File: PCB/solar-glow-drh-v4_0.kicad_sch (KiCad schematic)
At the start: 68 parts, among them J1 UPDI hdr, Q2 BSS138LT1G, SW2 LED master, U1 AVR64EA28 (VQFN28), U3 ADXL367, U5 NT3H2211, U6 TPS22919, U7 MB85RC512TY, U8 AEM10300, U9 TPS7A0233PDQNR

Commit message: Q2 + C9 low-profile respins, schematic side -- SOT-523 FET and 1206 C0G
The height ladder above 1.00 (supercaps aside) was C9 1.25 / Q2 1.20 /
U6 1.10. U6 stays (its only flatter variant is a DSBGA, hostile to
rework); these two come down. Both verified against their manufacturers'
own sheets before a field moved, per the U6-pin-map lesson:

Q2: BSS138LT1G (SOT-23, 1.20) -> DMG1012T-7 (SOT523, A1+A2 = 0.90 max,
DS31783 Rev 8-2). Same G/S/D pad order as SOT-23 so the symbol's pin map
carries over -- footprint-only swap for the copper. Electrically a step
up for this job: Vth 0.5-1.0 V (BSS138: 1.5 max) at the 3.3 V gate,
Idss 100 nA max on the drain the harvest budget sees, VGSS +/-6 V
(ESD-protected gate) with margin over the 3.3 V drive. 171k in stock.

C9: QSCT251Q470G1GV001E (0805 High-Q, 1.17 max) -> KGM31BCG2H470GT
(1206 C0G, Kyocera's own table: KGM31 = 3.2x1.6, thickness letter B =
0.94 MAX, and the 47 pF/500 V cell is a B part). Same 47 pF +/-2% -- the
tank tune math in the Description is untouched -- voltage doubles to
500 V, and the raw cap-Q spec drop vs the RF-grade Johanson is
immaterial in-circuit: the tank's loaded Q is coil-dominated. Reuses the
C25-C27 HandSolder land (solarglow:C_1206_3216Metric_HS_LP085), whose
0.95 model covers the 0.94 body -- the package-generic declaration C9's
own part_heights comment already blesses. 1,163 in stock.

The split workflow (fields first, DRH's copper later) now has a home in
the consistency check instead of a red CI: PENDING_FOOTPRINT_SYNC in
check_consistency.py declares the exact (sch_fp, board_fp) pair per ref
with its reason. The declared pair reports as a note; any other mismatch
stays a hard error; and a STALE entry (the board synced, or either side
changed) errors, so the ledger dies in the same commit as the board
round -- the FRONT_SIDE-snapshot shape, again.

Both datasheets fetched to the shelf (Q2 DS31783, C9 C0GNP0-KGM) at
their live prices; availability table regenerated, 29/29 lines OK;
PCB/README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
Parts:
- C9: footprint Capacitor_SMD:C_0805_2012Metric -> solarglow:C_1206_3216Metric_HS_LP085; MPN QSCT251Q470G1GV001E -> KGM31BCG2H470GT; Manufacturer Johanson Technology -> KYOCERA AVX; Supplier P/N 712-QSCT251Q470G1GV001ETR-ND -> 478-KGM31BCG2H470GTCT-ND
- Q2: value BSS138LT1G -> DMG1012T; footprint Package_TO_SOT_SMD:SOT-23 -> Package_TO_SOT_SMD:SOT-523; MPN BSS138LT1G -> DMG1012T-7; Manufacturer onsemi -> Diodes Incorporated; Supplier P/N BSS138LT1GOSCT-ND -> DMG1012T-7DICT-ND
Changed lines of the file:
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@@
 			)
 		)
-		(property "Value" "BSS138LT1G"
+		(property "Value" "DMG1012T"
 			(at 945.94 382.27 0)
 			(show_name no)
@@
 			)
 		)
-		(property "Footprint" "Package_TO_SOT_SMD:SOT-23"
+		(property "Footprint" "Package_TO_SOT_SMD:SOT-523"
 			(at 945.94 387.35 0)
 			(show_name no)
@@
 			)
 		)
-		(property "Description" "N-ch MOSFET SOT-23 -- EN_STO_CH low-side charge-disable buffer: gate<-PA4 (CHG_DIS_G), drain->EN_STO_CH, source->GND (cold-start-deadlock fix)"
+		(property "Description" "N-ch MOSFET SOT-523 (DMG1012T, 0.90 max -- low-profile respin 2026-08-06; was BSS138 SOT-23, 1.20) -- EN_STO_CH low-side charge-disable buffer: gate<-PA4 (CHG_DIS_G), drain->EN_STO_CH, source->GND (cold-start-deadlock fix). Same G/S/D pad order as SOT-23; Vth 1.0 max, Idss 100 nA max, VGSS +/-6 (ESD-protected gate)"
 			(at 934.72 372.11 0)
 			(show_name no)
@@
 			)
 		)
-		(property "MPN" "BSS138LT1G"
+		(property "MPN" "DMG1012T-7"
 			(at 934.72 372.11 0)
 			(show_name no)
@@
 			)
 		)
-		(property "Manufacturer" "onsemi"
+		(property "Manufacturer" "Diodes Incorporated"
 			(at 934.72 372.11 0)
 			(hide yes)
@@
 			)
 		)
-		(property "Supplier P/N" "BSS138LT1GOSCT-ND"
+		(property "Supplier P/N" "DMG1012T-7DICT-ND"
 			(at 934.72 372.11 0)
 			(hide yes)
@@
 			)
 		)
-		(property "Footprint" "Capacitor_SMD:C_0805_2012Metric"
+		(property "Footprint" "solarglow:C_1206_3216Metric_HS_LP085"
 			(at 571.5 129.54 0)
 			(hide yes)
@@
 			)
 		)
-		(property "Description" "NFC tank trim, 0805 high-Q C0G +/-2% (Johanson S-series, ultra-low ESR). PLACED at assembly as of 2026-07-30 - value derived, not trimmed: coil L = 0.958 uH by Greenhouse on the board's 7 rails, ferrite-loaded 1.05-1.30 uH, tag Ci = 50 pF (NT3H2211 Table 42), antenna Cc = 6 pF (AN11276 Table 2). 47 pF lands the enclosed resonance at 14.45 MHz against AN11276 4.2.1's 14.5 MHz single-tag target and stays above the 13.56 carrier across the whole ferrite range. Was 82 pF + DNP, which sat at 12.5 MHz enclosed - under the carrier, the wrong side to miss on."
+		(property "Description" "NFC tank trim, 1206 C0G 500 V +/-2% (Kyocera KGM31B, 0.94 max -- low-profile respin 2026-08-06; was Johanson 0805 High-Q QSCT, 1.17 max: raw cap-Q spec is lower than the RF-grade part but the tank's loaded Q is coil-dominated, and V doubles). PLACED at assembly as of 2026-07-30 - value derived, not trimmed: coil L = 0.958 uH by Greenhouse on the board's 7 rails, ferrite-loaded 1.05-1.30 uH, tag Ci = 50 pF (NT3H2211 Table 42), antenna Cc = 6 pF (AN11276 Table 2). 47 pF lands the enclosed resonance at 14.45 MHz against AN11276 4.2.1's 14.5 MHz single-tag target and stays above the 13.56 carrier across the whole ferrite range. Was 82 pF + DNP, which sat at 12.5 MHz enclosed - under the carrier, the wrong side to miss on."
 			(at 560.07 119.38 0)
 			(hide yes)
@@
 			)
 		)
-		(property "MPN" "QSCT251Q470G1GV001E"
+		(property "MPN" "KGM31BCG2H470GT"
 			(at 560.07 119.38 0)
 			(hide yes)
@@
 			)
 		)
-		(property "Manufacturer" "Johanson Technology"
+		(property "Manufacturer" "KYOCERA AVX"
 			(at 560.07 119.38 0)
 			(hide yes)
@@
 			)
 		)
-		(property "Supplier P/N" "712-QSCT251Q470G1GV001ETR-ND"
+		(property "Supplier P/N" "478-KGM31BCG2H470GTCT-ND"
 			(at 560.07 119.38 0)
 			(hide yes)

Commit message: C9: the Kyocera 1206 falls to the purpose-built answer -- Johanson QSCP 0603
DRH asked for an RF-grade part and widened the search to any case size.
The full-field sweep settled it: Johanson's High-Q family has NO 1206
(the case ladder runs 0201 -> 0603 -> 0805 -> 1111, and the 1111 is a
2.59 mm brick), no maker stocks a purpose-built RF 1206 under 1 mm, and
the uncommon cases (0505, 1111) all start at 1.27 thick. The flat,
+/-2%, >=250 V RF world lives entirely at 0603: Johanson QSCP (0.89),
Murata GQM18 (0.80), Kyocera/ATC 600S (0.89, $2.08).

Picked QSCP251Q470G1GV001T -- the SAME S-series as the QSCT fitted
today (Johanson's own sheet: legacy 251R14S470GV4T, 0603, 250 V,
47 pF +/-2%, thickness max 0.035 in = 0.89 mm), so the tank keeps its
exact pedigree, one case down instead of up. 43,680 in stock, $0.37.
The Kyocera KGM pick from the previous commit is superseded before any
copper moved: sch fields, PENDING_FOOTPRINT_SYNC pair (now 0805 ->
C_0603_1608Metric -- the rework SHRINKS the land, and the board already
hand-works 0603 at C22/C23/FB1/R15/R16), PCB/README row, and the shelf
(KGM sheet culled same-day, git history; JTI part sheet in at the live
price). Value stays 47 pF -- the tune math is untouched.

Availability table regenerated (29/29, C9 verified live); ERC at the
3-hit baseline; consistency 0/0 with the C9 transient re-declared.

Co-Authored-By: Claude Fable 5 <noreply@anthropic.com>
Claude-Session: https://claude.ai/code/session_015D4iTho3BuNxSQyJmyaxvg
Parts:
- C9: footprint solarglow:C_1206_3216Metric_HS_LP085 -> Capacitor_SMD:C_0603_1608Metric; MPN KGM31BCG2H470GT -> QSCP251Q470G1GV001T; Manufacturer KYOCERA AVX -> Johanson Technology; Supplier P/N 478-KGM31BCG2H470GTCT-ND -> 712-QSCP251Q470G1GV001TCT-ND
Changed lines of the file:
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@@
 			)
 		)
-		(property "Footprint" "solarglow:C_1206_3216Metric_HS_LP085"
+		(property "Footprint" "Capacitor_SMD:C_0603_1608Metric"
 			(at 571.5 129.54 0)
 			(hide yes)
@@
 			)
 		)
-		(property "Description" "NFC tank trim, 1206 C0G 500 V +/-2% (Kyocera KGM31B, 0.94 max -- low-profile respin 2026-08-06; was Johanson 0805 High-Q QSCT, 1.17 max: raw cap-Q spec is lower than the RF-grade part but the tank's loaded Q is coil-dominated, and V doubles). PLACED at assembly as of 2026-07-30 - value derived, not trimmed: coil L = 0.958 uH by Greenhouse on the board's 7 rails, ferrite-loaded 1.05-1.30 uH, tag Ci = 50 pF (NT3H2211 Table 42), antenna Cc = 6 pF (AN11276 Table 2). 47 pF lands the enclosed resonance at 14.45 MHz against AN11276 4.2.1's 14.5 MHz single-tag target and stays above the 13.56 carrier across the whole ferrite range. Was 82 pF + DNP, which sat at 12.5 MHz enclosed - under the carrier, the wrong side to miss on."
+		(property "Description" "NFC tank trim, 0603 High-Q C0G 250 V +/-2% (Johanson S-series QSCP, 0.89 max, legacy 251R14S470GV4T -- low-profile respin 2026-08-06, purpose-built RF part kept per DRH: the S-series has NO 1206 case and no maker stocks a flat RF 1206, so the same family one case DOWN. Was the 0805 QSCT, 1.17 max; the 2026-07-30 0402->0805 upsize fled 0402 rework, and 0603 is the board's workhorse hand case). PLACED at assembly as of 2026-07-30 - value derived, not trimmed: coil L = 0.958 uH by Greenhouse on the board's 7 rails, ferrite-loaded 1.05-1.30 uH, tag Ci = 50 pF (NT3H2211 Table 42), antenna Cc = 6 pF (AN11276 Table 2). 47 pF lands the enclosed resonance at 14.45 MHz against AN11276 4.2.1's 14.5 MHz single-tag target and stays above the 13.56 carrier across the whole ferrite range. Was 82 pF + DNP, which sat at 12.5 MHz enclosed - under the carrier, the wrong side to miss on."
 			(at 560.07 119.38 0)
 			(hide yes)
@@
 			)
 		)
-		(property "MPN" "KGM31BCG2H470GT"
+		(property "MPN" "QSCP251Q470G1GV001T"
 			(at 560.07 119.38 0)
 			(hide yes)
@@
 			)
 		)
-		(property "Manufacturer" "KYOCERA AVX"
+		(property "Manufacturer" "Johanson Technology"
 			(at 560.07 119.38 0)
 			(hide yes)
@@
 			)
 		)
-		(property "Supplier P/N" "478-KGM31BCG2H470GTCT-ND"
+		(property "Supplier P/N" "712-QSCP251Q470G1GV001TCT-ND"
 			(at 560.07 119.38 0)
 			(hide yes)

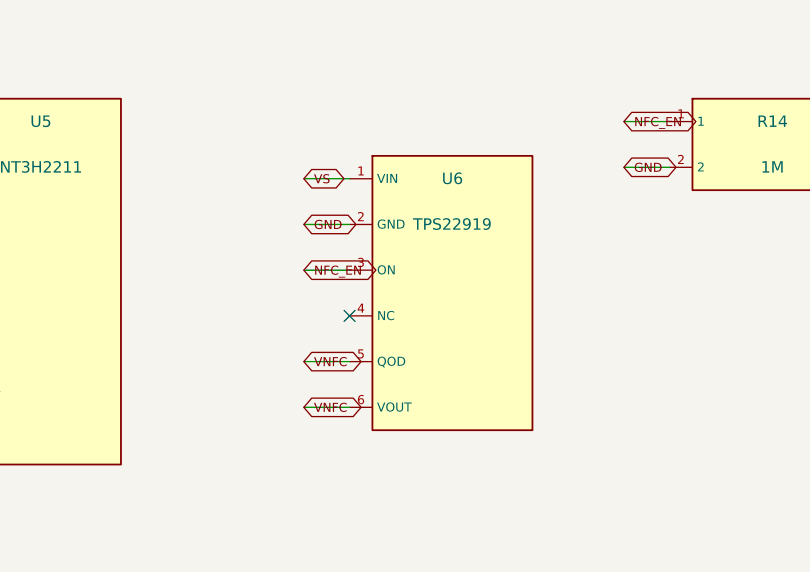
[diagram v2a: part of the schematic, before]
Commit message: U6 goes DSBGA: TPS22916C, 0.5 mm -- every component now clears 1.1 for the ultrathin card
DRH called the swap: with C25-C27 at 0.95, Q2 at 0.90 and C9 at 0.89
pending, U6's SC-70 (1.10) was the last non-supercap part at the 1.1
line, and the ultrathin-card option wants everything UNDER it. The
TPS22919 has no BGA variant (SLVSEN5B lists DCK only); the sibling
that exists for exactly this is the TPS22916 -- TI's ultra-low-leakage
WCSP load switch. C version chosen deliberately: active-high ON, 150R
QOD (the 22919 has QOD; CN/CNL delete it), slow inrush-limited ramp
(the 22919's controlled rise, same idea), plus reverse-current
blocking the 22919 never had.

The honest trade, both sheets side by side: ISD 10 nA typ / 100 nA max
(-40..85) vs the 22919's 2 nA typ -- +8 nA typical on the OFF state the
switch lives in, ~26 nW at 3.3 V -- bought back 16x in ON-state IQ
(0.5 uA vs 8 uA) and 0.6 mm of height. VIN 1-5.5 V, RON 70 mOhm at
3.6 V, ON-pin leakage 10 nA max driven high; R14's 1 M pulldown keeps
the hard-off default either way.

Schematic surgery (the 6-pin symbol dies, a 4-ball one replaces it):
new solarglow:U6_TPS22916 lib def with balls A2/B1/B2/A1 positioned on
the OLD pins 1/2/3/6 canvas points, so the VS/GND/NFC_EN/VNFC wires
never move; the QOD stub wire + its VNFC label deleted (QOD is
internal now) and pin 4's no_connect marker with it -- ERC stays at
the 3-hit baseline, no dangles. The old solarglow:U6 lib def is gone
outright: an unused lib def with part-number defaults is exactly the
bait that sold C1 as an LDO this morning.

Footprint minted from TI's own drawing (solarglow:TPS22916_YFP0004,
4223507/A + SLVSDO5F example layout): 4x diam 0.23 NSMD circles on
0.4 mm pitch, mask +0.05/side, pad-to-pad air 0.17 >= the 0.152 floor,
A1 corner marked on F.Fab. Model chain complete in the same commit:
TI_DSBGA4_YFP.step (0.81 sq x 0.50 max, spec body) + part_colors
entry, referenced by the footprint itself -- no ATTACH map needed.

Ledgers: PENDING_FOOTPRINT_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
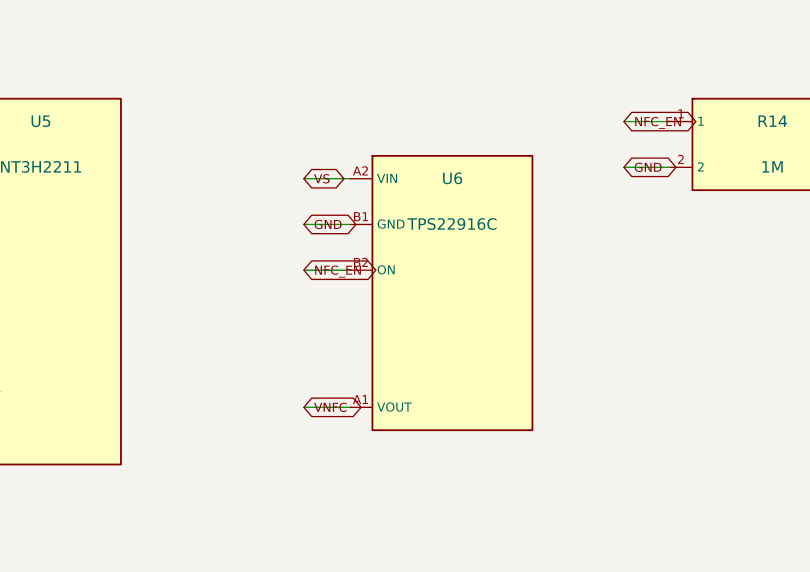
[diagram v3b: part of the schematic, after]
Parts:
- U6: value TPS22919 -> TPS22916C; footprint Package_TO_SOT_SMD:SOT-363_SC-70-6 -> solarglow:TPS22916_YFP0004; symbol solarglow:U6 -> solarglow:U6_TPS22916; MPN TPS22919DCKR -> TPS22916CYFPR; Supplier P/N 296-TPS22919DCKRCT-ND -> 296-50065-1-ND
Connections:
- net GND: now also U6.B1 (GND); no longer U6.2 (GND)
- net NFC_EN: now also U6.B2 (ON); no longer U6.3 (ON)
- net VNFC: now also U6.A1 (VOUT); no longer U6.5 (QOD), U6.6 (VOUT)
- net VS: now also U6.A2 (VIN); no longer U6.1 (VIN)
- no-connect marks 19 -> 18
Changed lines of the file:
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@@
 	)
 	(no_connect
-		(at 650.24 91.44)
-	)
-	(no_connect
 		(at 459.74 499.11)
 	)
@@
 	(wire
 		(pts
-			(xy 650.24 96.52) (xy 645.16 96.52)
-		)
-		(stroke
-			(width 0)
-			(type default)
-		)
-	)
-	(wire
-		(pts
 			(xy 279.4 241.3) (xy 274.32 241.3)
 		)
@@
 		)
 	)
-	(global_label "VNFC"
-		(shape bidirectional)
-		(at 645.16 96.52 0)
-		(effects
-			(font
-				(size 1 1)
-			)
-		)
-		(property "Intersheetrefs" "${INTERSHEET_REFS}"
-			(at 645.16 96.52 0)
-			(hide yes)
-			(show_name no)
-			(do_not_autoplace no)
-			(effects
-				(font
-					(size 1.27 1.27)
-				)
-			)
-		)
-	)
 	(global_label "LDRV1"
 		(shape bidirectional)
@@
 	)
 	(symbol
-		(lib_id "solarglow:U6")
+		(lib_id "solarglow:U6_TPS22916")
 		(at 650.24 76.2 0)
 		(unit 1)
@@
 			)
 		)
-		(property "Value" "TPS22919"
+		(property "Value" "TPS22916C"
 			(at 661.67 81.28 0)
 			(show_name no)
@@
 			)
 		)
-		(property "Footprint" "Package_TO_SOT_SMD:SOT-363_SC-70-6"
+		(property "Footprint" "solarglow:TPS22916_YFP0004"
 			(at 661.67 86.36 0)
 			(hide yes)
@@
 			)
 		)
-		(property "Datasheet" "SLVSEN5B"
+		(property "Datasheet" "SLVSDO5F"
 			(at 650.24 76.2 0)
 			(hide yes)
@@
 			)
 		)
-		(property "Description" "NFC VNFC high-side load switch - TPS22919 (SC-70-6). ISD 2nA typ / 20nA max @25C vs the 917's 10nA typ / 100nA max, so better where the card lives; its 800nA max applies only at +125C, where the 917 specifies nothing at all. IQ 8uA typ while ON is a one-shot, not a standing cost: provisioning runs once at cold boot (~157ms), i.e. 3.9uJ against a 9.8J tank. Pin-for-pin with the 917 on every net used - pin4 CT-float becomes NC-float, QOD->VOUT sanctioned (internal 24 ohm), active-HIGH ON. Losses: no reverse-current blocking, and a fixed 1.75ms ramp (NFC_SOFTSTART_US raised to 2000). AEC-Q100 exists as TPS22919QDCKRQ1; the 917 has no -Q1 in any package."
+		(property "Description" "Ultra-low-leakage load switch for the NFC tag rail. TPS22916C DSBGA-4 YFP (0.4 mm pitch, 0.5 max height -- the 2026-08-06 ultrathin swap; was TPS22919 SC-70-6, 1.1). C version = active-high ON, 150R QOD, slow inrush-limited ramp, reverse-current blocking. ISD 10 nA typ/100 nA max vs the 22919 2 nA typ -- +8 nA typ on the dominant OFF state, bought back 16x in ON-state IQ (0.5 uA vs 8 uA); ball map A1 VOUT, A2 VIN, B1 GND, B2 ON per SLVSDO5F Fig 5-2."
 			(at 650.24 76.2 0)
 			(hide yes)
@@
 			)
 		)
-		(property "MPN" "TPS22919DCKR"
+		(property "MPN" "TPS22916CYFPR"
 			(at 650.24 76.2 0)
 			(hide yes)
@@
 			)
 		)
-		(property "Supplier P/N" "296-TPS22919DCKRCT-ND"
+		(property "Supplier P/N" "296-50065-1-ND"
 			(at 459.74 372.11 0)
 			(hide yes)
@@
 			)
 		)
-		(pin "1"
-		)
-		(pin "2"
-		)
-		(pin "3"
+		(pin "A1"
 		)
-		(pin "4"
+		(pin "A2"
 		)
-		(pin "5"
+		(pin "B1"
 		)
-		(pin "6"
+		(pin "B2"
 		)
 		(instances

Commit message: TC1 grows a debug face: pads 4-6 to BTN/SDA/SCL -- one cable programs, powers, talks I2C and wakes the card
The three unused Tag-Connect pads stop being dead copper. Pad 5 = SDA,
pad 6 = SCL (the bus gets its own row); pad 4 = BTN, deliberately beside
pad 3 = GND so shorting the two middle pads is the manual wake gesture
on bare pads. BTN was already a named single-node stub on PA5 -- the
documented future-button path -- so this lands designed intent rather
than inventing a net: the bench gets a scriptable, active-low wake line
where the accelerometer's tap was the only (unautomatable) stimulus.

TC1/b1 gets the identical assignment -- the B-side mirror stays a true
copy, or it lies about what a cable on that side can do.

Schematic side only, DRH routes the copper: same transient class as the
U6/Q2/C9 swaps (kibot's parity gate holds the board round hostage until
the rework upload; the consistency parity check compares footprint
assignments, which are untouched here). Six no_connects out, six
wire+label pairs in, house style, CRLF preserved. ERC 0/0 before and
after; consistency 20/20 green; netlist shows all six joins with the
mirror byte-identical.

Co-Authored-By: Claude Fable 5 <noreply@anthropic.com>
Claude-Session: https://claude.ai/code/session_015D4iTho3BuNxSQyJmyaxvg
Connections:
- net BTN: now also TC1.4, TC1/b1.4
- net SCL: now also TC1.6, TC1/b1.6
- net SDA: now also TC1.5, TC1/b1.5
- no-connect marks 18 -> 12
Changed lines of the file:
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@@
 	)
 	(no_connect
-		(at 410.21 139.7)
-	)
-	(no_connect
 		(at 459.74 499.11)
 	)
@@
 		(at 209.55 144.78)
 	)
-	(no_connect
-		(at 410.21 176.53)
-	)
-	(no_connect
-		(at 410.21 134.62)
-	)
 		(no_connect
 		(at 209.55 114.3)
@@
 	)
 	(no_connect
-		(at 410.21 144.78)
-	)
-	(no_connect
 		(at 209.55 104.14)
 	)
@@
 	)
 	(no_connect
-		(at 410.21 166.37)
-	)
-	(no_connect
 		(at 459.74 448.31)
 	)
@@
 		(at 604.52 100.33)
 	)
-	(no_connect
-		(at 410.21 171.45)
-	)
 	(wire
 		(pts
@@
 				)
 			)
+		)
+	)
+	(wire
+		(pts
+			(xy 410.21 134.62) (xy 405.13 134.62)
+		)
+		(stroke
+			(width 0)
+			(type default)
+		)
+	)
+	(global_label "BTN"
+		(shape bidirectional)
+		(at 405.13 134.62 0)
+		(effects
+			(font
+				(size 1 1)
+			)
+		)
+		(property "Intersheetrefs" "${INTERSHEET_REFS}"
+			(at 405.13 134.62 0)
+			(hide yes)
+			(show_name no)
+			(do_not_autoplace no)
+			(effects
+				(font
+					(size 1.27 1.27)
+				)
+			)
+		)
+	)
+	(wire
+		(pts
+			(xy 410.21 139.7) (xy 405.13 139.7)
+		)
+		(stroke
+			(width 0)
+			(type default)
+		)
+	)
+	(global_label "SDA"
+		(shape bidirectional)
+		(at 405.13 139.7 0)
+		(effects
+			(font
+				(size 1 1)
+			)
+		)
+		(property "Intersheetrefs" "${INTERSHEET_REFS}"
+			(at 405.13 139.7 0)
+			(hide yes)
+			(show_name no)
+			(do_not_autoplace no)
+			(effects
+				(font
+					(size 1.27 1.27)
+				)
+			)
+		)
+	)
+	(wire
+		(pts
+			(xy 410.21 144.78) (xy 405.13 144.78)
+		)
+		(stroke
+			(width 0)
+			(type default)
+		)
+	)
+	(global_label "SCL"
+		(shape bidirectional)
+		(at 405.13 144.78 0)
+		(effects
+			(font
+				(size 1 1)
+			)
+		)
+		(property "Intersheetrefs" "${INTERSHEET_REFS}"
+			(at 405.13 144.78 0)
+			(hide yes)
+			(show_name no)
+			(do_not_autoplace no)
+			(effects
+				(font
+					(size 1.27 1.27)
+				)
+			)
+		)
+	)
+	(wire
+		(pts
+			(xy 410.21 166.37) (xy 405.13 166.37)
+		)
+		(stroke
+			(width 0)
+			(type default)
+		)
+	)
+	(global_label "BTN"
+		(shape bidirectional)
+		(at 405.13 166.37 0)
+		(effects
+			(font
+				(size 1 1)
+			)
+		)
+		(property "Intersheetrefs" "${INTERSHEET_REFS}"
+			(at 405.13 166.37 0)
+			(hide yes)
+			(show_name no)
+			(do_not_autoplace no)
+			(effects
+				(font
+					(size 1.27 1.27)
+				)
+			)
+		)
+	)
+	(wire
+		(pts
+			(xy 410.21 171.45) (xy 405.13 171.45)
+		)
+		(stroke
+			(width 0)
+			(type default)
+		)
+	)
+	(global_label "SDA"
+		(shape bidirectional)
+		(at 405.13 171.45 0)
+		(effects
+			(font
+				(size 1 1)
+			)
+		)
+		(property "Intersheetrefs" "${INTERSHEET_REFS}"
+			(at 405.13 171.45 0)
+			(hide yes)
+			(show_name no)
+			(do_not_autoplace no)
+			(effects
+				(font
+					(size 1.27 1.27)
+				)
+			)
+		)
+	)
+	(wire
+		(pts
+			(xy 410.21 176.53) (xy 405.13 176.53)
+		)
+		(stroke
+			(width 0)
+			(type default)
+		)
+	)
+	(global_label "SCL"
+		(shape bidirectional)
+		(at 405.13 176.53 0)
+		(effects
+			(font
+				(size 1 1)
+			)
+		)
+		(property "Intersheetrefs" "${INTERSHEET_REFS}"
+			(at 405.13 176.53 0)
+			(hide yes)
+			(show_name no)
+			(do_not_autoplace no)
+			(effects
+				(font
+					(size 1.27 1.27)
+				)
+			)
